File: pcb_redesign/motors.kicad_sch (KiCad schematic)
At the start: 8 parts

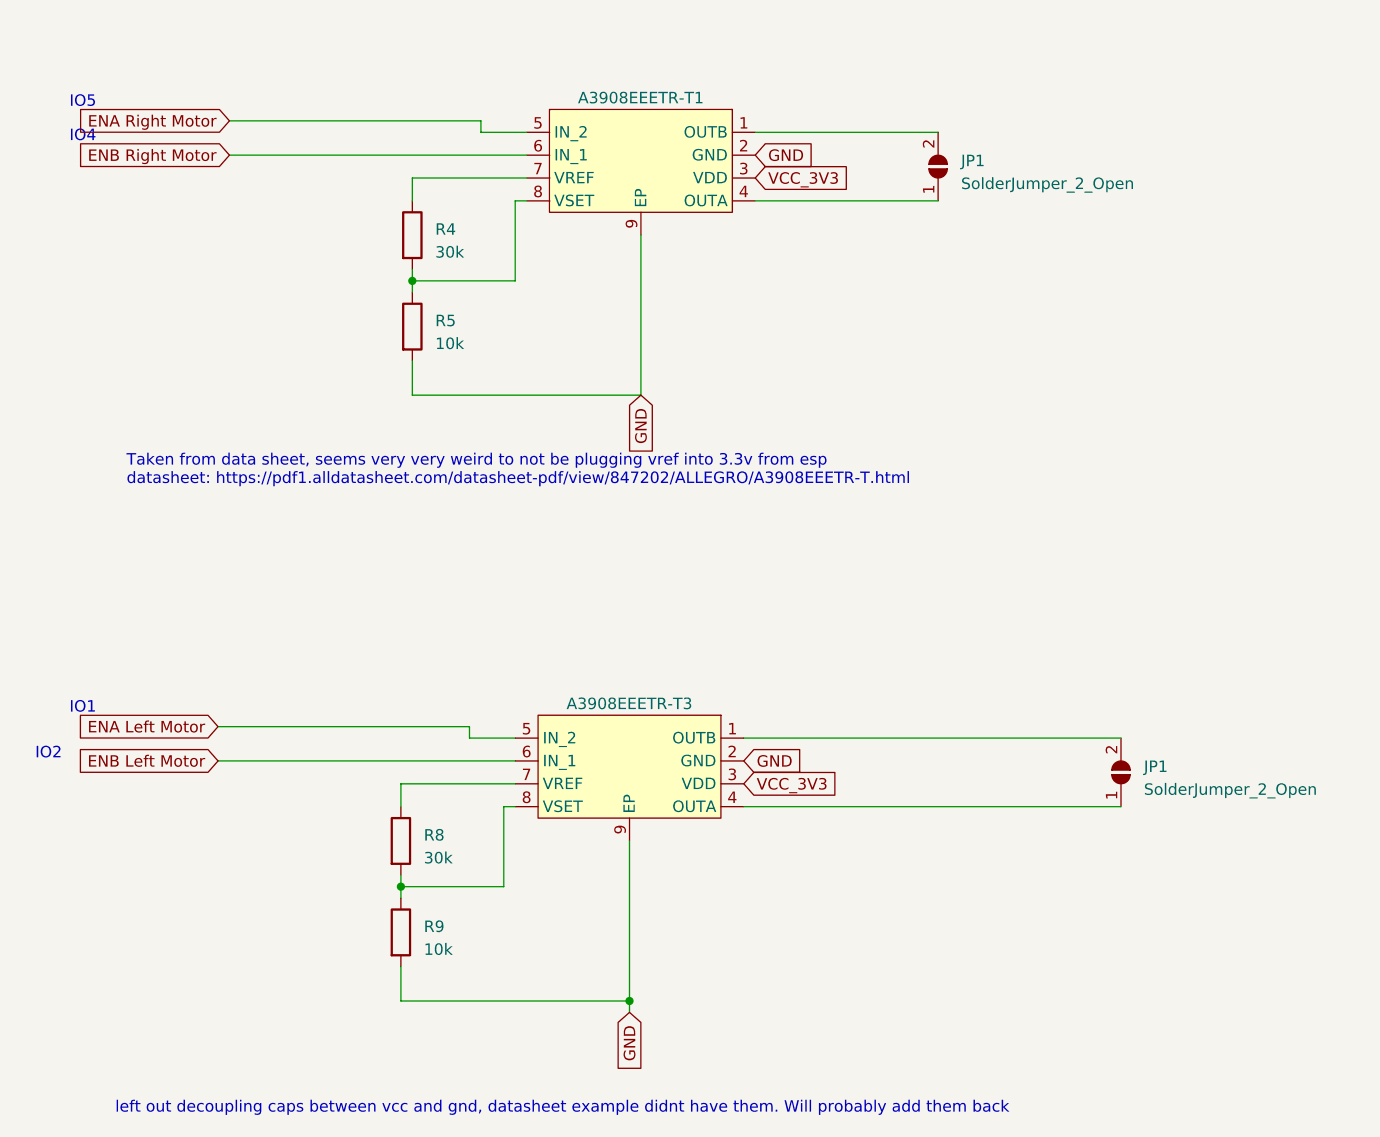
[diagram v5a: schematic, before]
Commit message: finished adding decoupling caps, shipped off to jlc
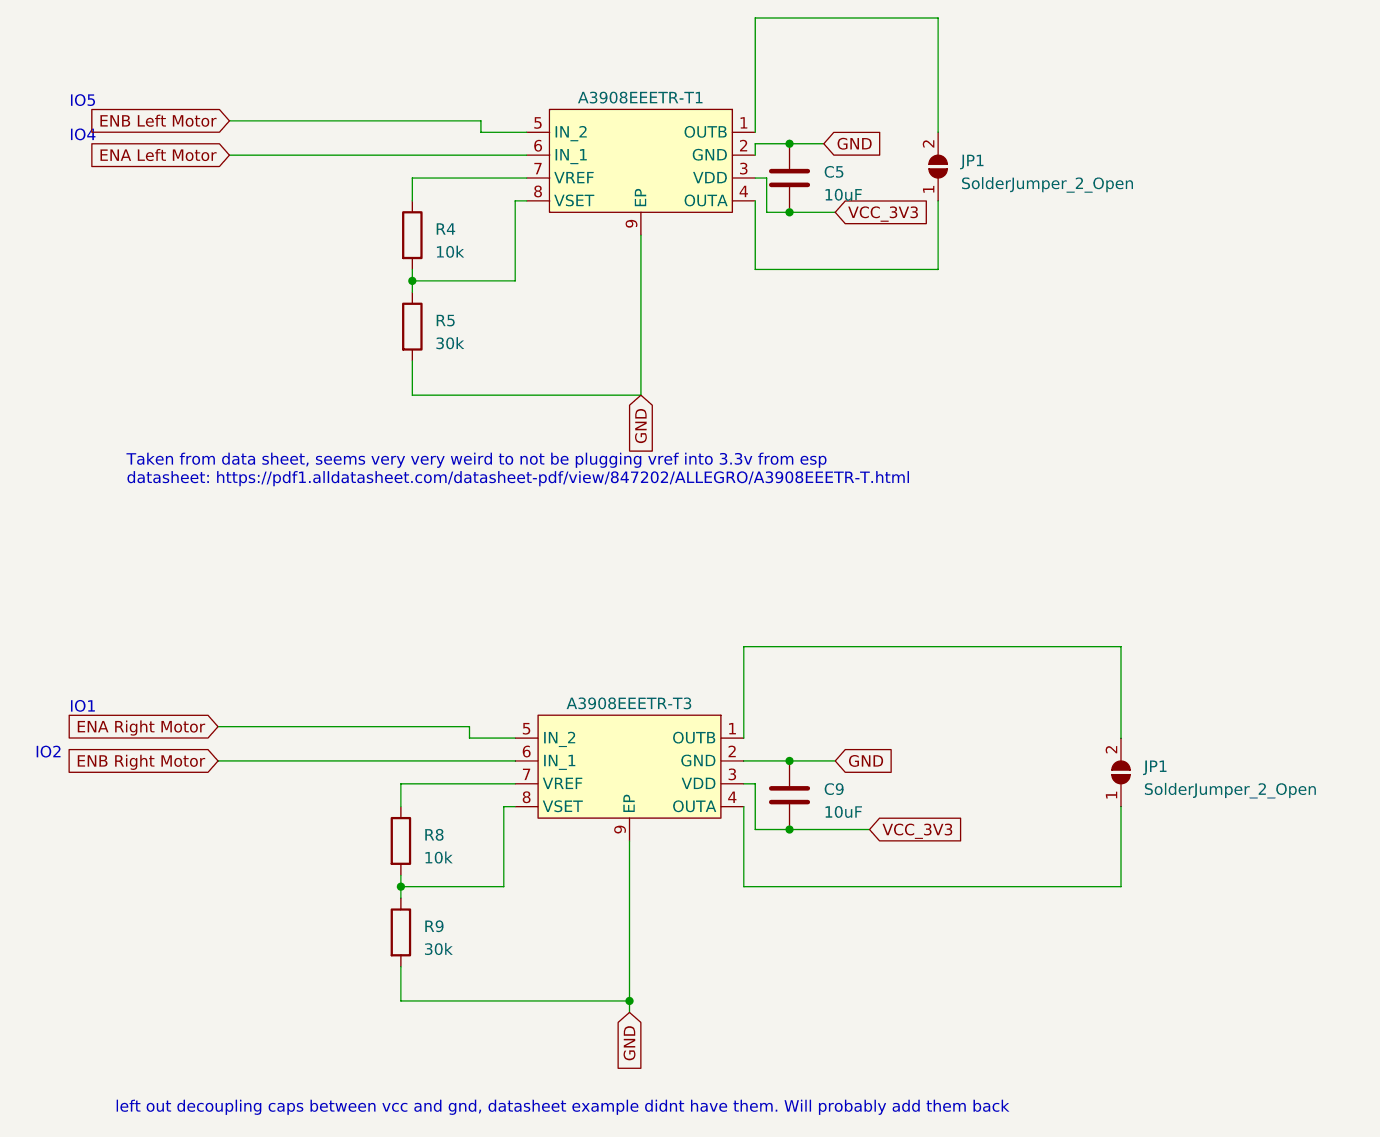
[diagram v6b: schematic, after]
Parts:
- added C5, C9: 10uF, Capacitor_SMD:C_0603_1608Metric, symbol Device:C
- R4, R8: value 30k -> 10k
- R5, R9: value 10k -> 30k
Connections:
- net ENA Left Motor: now also A3908EEETR-T1.6 (IN_1); no longer A3908EEETR-T3.5 (IN_2)
- net ENA Right Motor: now also A3908EEETR-T3.5 (IN_2); no longer A3908EEETR-T1.5 (IN_2)
- net ENB Left Motor: now also A3908EEETR-T1.5 (IN_2); no longer A3908EEETR-T3.6 (IN_1)
- net ENB Right Motor: now also A3908EEETR-T3.6 (IN_1); no longer A3908EEETR-T1.6 (IN_1)
- net GND: now also C5.1, C9.1
- net VCC_3V3: now also C5.2, C9.2
